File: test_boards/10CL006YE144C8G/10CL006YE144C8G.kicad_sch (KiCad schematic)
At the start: 90 parts, among them IC1 10CL006YE144C8G, J1 CL_JTAG, U1 W25Q128JVS, Y1 SG-7050CAN

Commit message: Полный рефакторинг. components может быть несколько. Используются поля KiCad для компонент
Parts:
- removed C41: 4.7 uF, Capacitor_SMD:C_0603_1608Metric_Pad1.08x0.95mm_HandSolder, symbol Device:C
- removed C50: 100 nF, Capacitor_SMD:C_0603_1608Metric_Pad1.08x0.95mm_HandSolder, symbol Device:C
- renumbered C42 to C41, C43 to C42, C44 to C43, C45 to C44, C46 to C45, C47 to C46, C48 to C47, C49 to C48, C51 to C49, C52 to C50, C53 to C51, C54 to C52, C55 to C53, C56 to C54, C57 to C55, C58 to C56, C59 to C57, C60 to C58, C61 to C59, C62 to C60, C63 to C61, C64 to C62, C65 to C63, C66 to C64, C67 to C65, C68 to C66, C69 to C67, C70 to C68

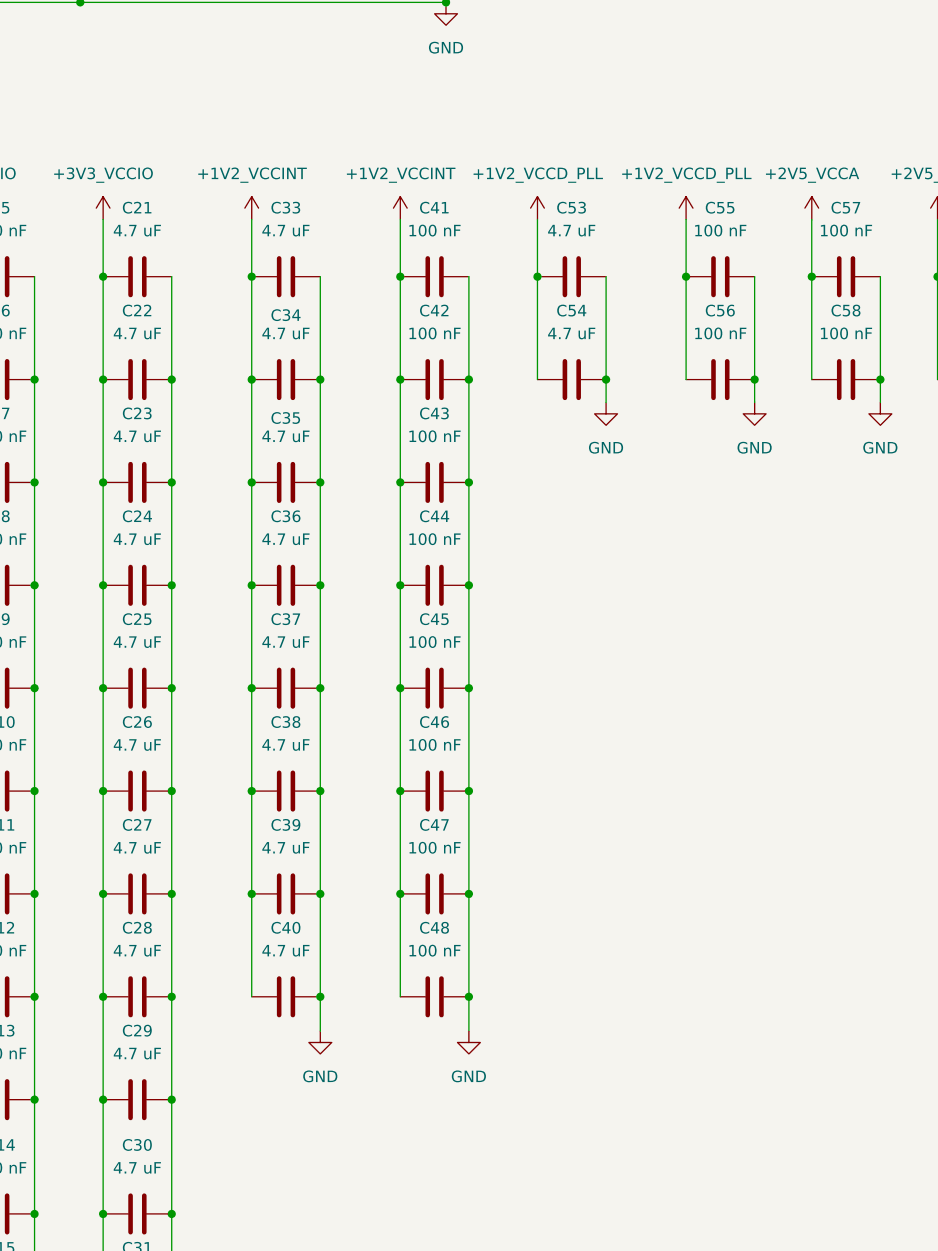
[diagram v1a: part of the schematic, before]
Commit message: Проект переименован в KiCadSpoke
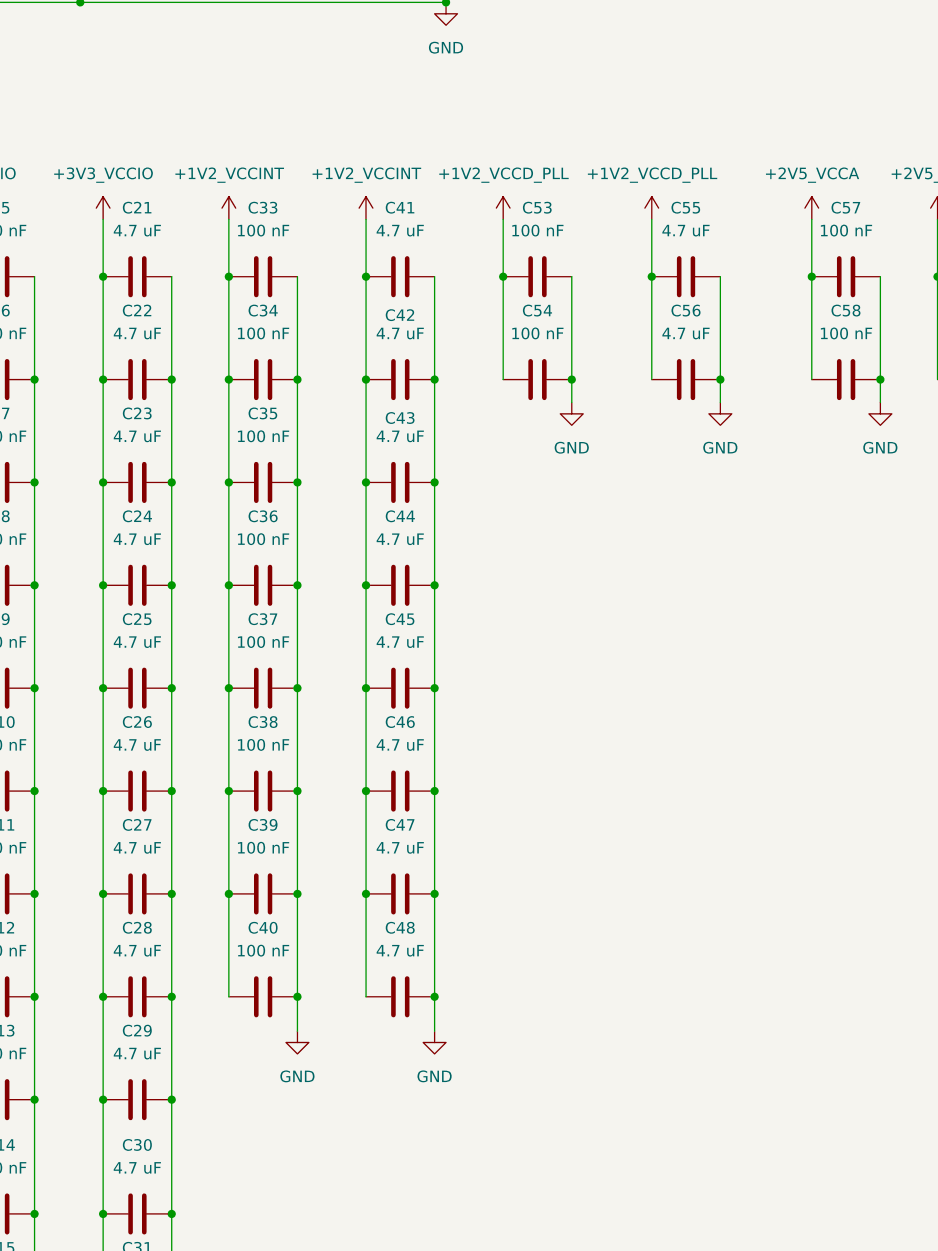
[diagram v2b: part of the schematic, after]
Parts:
- C10, C11, C12, C13, C14, C15, C16, C17, C18, C19, C20, C57, C58, C6, C7, C8, C9: Role (none) -> LIGHT; TemplateRole (none) -> LIGHT
- C21: Role (none) -> HEAVY; TemplateRole VCCIO1_LIGHT -> HEAVY
- C22, C23, C24, C25, C26, C27, C28, C29, C30, C31, C32, C59, C60: Role (none) -> HEAVY; TemplateRole (none) -> HEAVY
- C33: renamed from C41; Role (none) -> LIGHT; TemplateRole (none) -> LIGHT
- C34: renamed from C42; Role (none) -> LIGHT; TemplateRole (none) -> LIGHT
- C35: renamed from C43; Role (none) -> LIGHT; TemplateRole (none) -> LIGHT
- C36: renamed from C44; Role (none) -> LIGHT; TemplateRole (none) -> LIGHT
- C37: renamed from C45; Role (none) -> LIGHT; TemplateRole (none) -> LIGHT
- C38: renamed from C46; Role (none) -> LIGHT; TemplateRole (none) -> LIGHT
- C39: renamed from C47; Role (none) -> LIGHT; TemplateRole (none) -> LIGHT
- C40: renamed from C48; Role (none) -> LIGHT; TemplateRole (none) -> LIGHT
- C41: renamed from C33; Role (none) -> HEAVY; TemplateRole (none) -> HEAVY
- C42: renamed from C34; Role (none) -> HEAVY; TemplateRole (none) -> HEAVY
- C43: renamed from C35; Role (none) -> HEAVY; TemplateRole (none) -> HEAVY
- C44: renamed from C36; Role (none) -> HEAVY; TemplateRole (none) -> HEAVY
- C45: renamed from C37; Role (none) -> HEAVY; TemplateRole (none) -> HEAVY
- C46: renamed from C38; Role (none) -> HEAVY; TemplateRole (none) -> HEAVY
- C47: renamed from C39; Role (none) -> HEAVY; TemplateRole (none) -> HEAVY
- C48: renamed from C40; Role (none) -> HEAVY; TemplateRole (none) -> HEAVY
- C5: Role (none) -> LIGHT; TemplateRole VCCIO1_HEAVY -> LIGHT
- C53: renamed from C55; Role (none) -> LIGHT; TemplateRole (none) -> LIGHT
- C54: renamed from C56; Role (none) -> LIGHT; TemplateRole (none) -> LIGHT
- C55: renamed from C53; Role (none) -> HEAVY; TemplateRole (none) -> HEAVY
- C56: renamed from C54; Role (none) -> HEAVY; TemplateRole (none) -> HEAVY
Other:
- moved on the sheet: C33, C34, C35, C36, C37, C38, C39, C40, C41, C42, C43, C44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
